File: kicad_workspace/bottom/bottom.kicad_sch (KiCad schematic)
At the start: 50 parts, among them J1 Battery connector, J2 Battery connector, M1 N20_MOTOR_EXTENDED_SHAFT, M2 N20_MOTOR_EXTENDED_SHAFT, U1 DRV8833PWP, U3 STM32F303RETx, U4 BNO055, Y1 32.768kHz, Y2 8MHz, Y3 32.768kHz

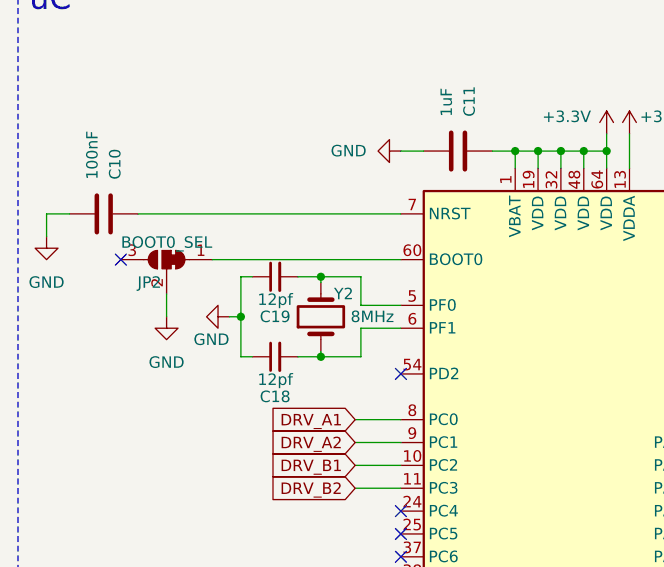
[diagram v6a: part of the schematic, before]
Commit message: initial stm and its elements placement
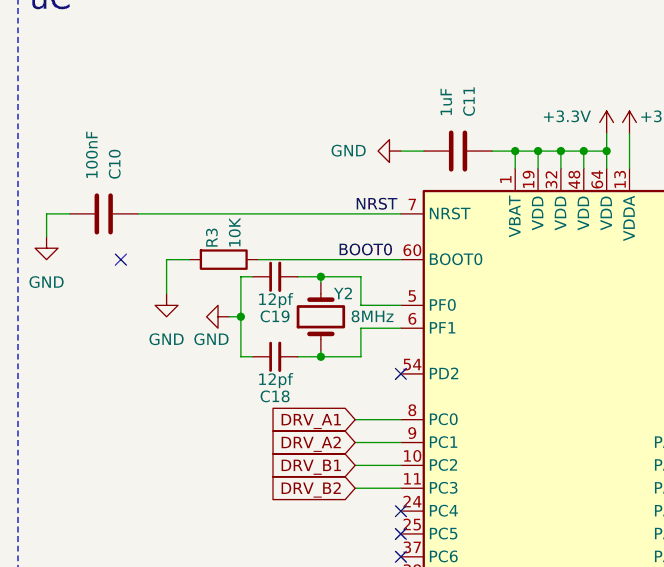
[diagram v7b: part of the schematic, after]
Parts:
- removed JP2: BOOT0_SEL, Jumper:SolderJumper-3_P1.3mm_Bridged12_Pad1.0x1.5mm_NumberLabels, symbol Jumper:SolderJumper_3_Bridged12
- added R3: 10K, Resistor_SMD:R_0805_2012Metric, symbol Device:R
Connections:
- net GND: now also R3.2
- net NRST: now reaches C10.1, U3.7 (NRST)
- net BOOT0: now reaches U3.60 (BOOT0)
- net BOOT0: now also R3.1
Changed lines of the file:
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@@
     (stroke (width 0) (type default))
   )
+  (wire (pts (xy 33.02 117.475) (xy 30.48 117.475))
+    (stroke (width 0) (type default))
+  )
   (wire (pts (xy 346.075 52.07) (xy 346.075 58.42))
     (stroke (width 0) (type default))
@@
     (stroke (width 0) (type default))
   )
-  (wire (pts (xy 35.56 117.475) (xy 56.515 117.475))
+  (wire (pts (xy 40.64 117.475) (xy 56.515 117.475))
     (stroke (width 0) (type default))
   )
@@
     (stroke (width 0) (type default))
   )
-  (wire (pts (xy 30.48 121.285) (xy 30.48 123.825))
+  (wire (pts (xy 30.48 117.475) (xy 30.48 121.285))
     (stroke (width 0) (type default))
   )
@@
     (effects (font (size 2.54 2.54)) (justify left bottom))
   )
+  (label "BOOT0" (at 49.53 117.475 0) (fields_autoplaced)
+    (effects (font (size 1.27 1.27)) (justify left bottom))
+  )
+  (label "NRST" (at 51.435 112.395 0) (fields_autoplaced)
+    (effects (font (size 1.27 1.27)) (justify left bottom))
+  )
   (global_label "DRV_A2" (shape input) (at 51.435 137.795 180) (fields_autoplaced)
     (effects (font (size 1.27 1.27)) (justify right))
@@
     )
   )
-  (symbol (lib_id "Jumper:SolderJumper_3_Bridged12") (at 30.48 117.475 0) (mirror y) (unit 1)
-    (in_bom yes) (on_board yes) (dnp no)
-    (property "Reference" "JP2" (at 28.575 120.015 0)
-      (effects (font (size 1.27 1.27)))
-    )
-    (property "Value" "BOOT0_SEL" (at 30.48 115.57 0)
-      (effects (font (size 1.27 1.27)))
-    )
-    (property "Footprint" "Jumper:SolderJumper-3_P1.3mm_Bridged12_Pad1.0x1.5mm_NumberLabels" (at 30.48 117.475 0)
-      (effects (font (size 1.27 1.27)) hide)
-    )
-    (property "Datasheet" "~" (at 30.48 117.475 0)
-      (effects (font (size 1.27 1.27)) hide)
-    )
-    (pin "1")
-    (pin "2")
-    (pin "3")
-    (instances
-      (project "bottom"
-        (path "/8949e4cc-98fb-401d-bf78-7a26c685fd98"
-          (reference "JP2") (unit 1)
-        )
-      )
-    )
-  )
   (symbol (lib_id "power:-BATT") (at 325.755 80.645 90) (unit 1)
     (in_bom yes) (on_board yes) (dnp no) (fields_autoplaced)
@@
     )
   )
-  (symbol (lib_id "power:GND") (at 30.48 123.825 0) (mirror y) (unit 1)
+  (symbol (lib_id "power:GND") (at 30.48 121.285 0) (mirror y) (unit 1)
     (in_bom yes) (on_board yes) (dnp no) (fields_autoplaced)
-    (property "Reference" "#PWR042" (at 30.48 130.175 0)
+    (property "Reference" "#PWR042" (at 30.48 127.635 0)
       (effects (font (size 1.27 1.27)) hide)
     )
-    (property "Value" "GND" (at 30.48 128.905 0)
+    (property "Value" "GND" (at 30.48 126.365 0)
       (effects (font (size 1.27 1.27)))
     )
-    (property "Footprint" "" (at 30.48 123.825 0)
+    (property "Footprint" "" (at 30.48 121.285 0)
       (effects (font (size 1.27 1.27)) hide)
     )
-    (property "Datasheet" "" (at 30.48 123.825 0)
+    (property "Datasheet" "" (at 30.48 121.285 0)
       (effects (font (size 1.27 1.27)) hide)
     )
@@
         )
       )
+    )
+  )
+  (symbol (lib_id "Device:R") (at 36.83 117.475 270) (unit 1)
+    (in_bom yes) (on_board yes) (dnp no)
+    (property "Reference" "R3" (at 35.56 116.205 0)
+      (effects (font (size 1.27 1.27)) (justify right))
+    )
+    (property "Value" "10K" (at 38.1 116.205 0)
+      (effects (font (size 1.27 1.27)) (justify right))
+    )
+    (property "Footprint" "Resistor_SMD:R_0805_2012Metric" (at 36.83 115.697 90)
+      (effects (font (size 1.27 1.27)) hide)
+    )
+    (property "Datasheet" "~" (at 36.83 117.475 0)
+      (effects (font (size 1.27 1.27)) hide)
+    )
+    (pin "1")
+    (pin "2")
+    (instances
+      (project "bottom"
+        (path "/8949e4cc-98fb-401d-bf78-7a26c685fd98"
+          (reference "R3") (unit 1)
+        )
+      )

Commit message: Add current render to readme. Fix some footprint 3d model paths problems
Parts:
- J1, J2: footprint Connector_JST:JST_XH_B2B-XH-AM_1x02_P2.50mm_Vertical -> Connector_JST:JST_XH_B2B-XH-A_1x02_P2.50mm_Vertical
- U1: footprint Package_SO:HTSSOP-16-1EP_4.4x5mm_P0.65mm_EP3.4x5mm_Mask2.46x2.31mm_ThermalVias -> Package_SO:TSSOP-16-1EP_4.4x5mm_P0.65mm_EP3x3mm_ThermalVias
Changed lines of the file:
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@@
       (effects (font (size 1.27 1.27)) (justify left))
     )
-    (property "Footprint" "Connector_JST:JST_XH_B2B-XH-AM_1x02_P2.50mm_Vertical" (at 282.575 25.4 0)
+    (property "Footprint" "Connector_JST:JST_XH_B2B-XH-A_1x02_P2.50mm_Vertical" (at 282.575 25.4 0)
       (effects (font (size 1.27 1.27)) hide)
     )
@@
       (effects (font (size 1.27 1.27)) (justify left))
     )
-    (property "Footprint" "Package_SO:HTSSOP-16-1EP_4.4x5mm_P0.65mm_EP3.4x5mm_Mask2.46x2.31mm_ThermalVias" (at 72.39 41.91 0)
+    (property "Footprint" "Package_SO:TSSOP-16-1EP_4.4x5mm_P0.65mm_EP3x3mm_ThermalVias" (at 72.39 41.91 0)
       (effects (font (size 1.27 1.27)) (justify left) hide)
     )
@@
       (effects (font (size 1.27 1.27)) (justify left))
     )
-    (property "Footprint" "Connector_JST:JST_XH_B2B-XH-AM_1x02_P2.50mm_Vertical" (at 282.575 31.115 0)
-      (effects (font (size 1.27 1.27)) hide)
-    )
+    (property "Footprint" "Connector_JST:JST_XH_B2B-XH-A_1x02_P2.50mm_Vertical" (at 282.575 31.115 0)
+      (effects (font (size 1.27 1.27)) hide)
+    )
